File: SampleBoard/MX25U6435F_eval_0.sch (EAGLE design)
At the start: 7 parts, among them CN1 ARDUINO_COMPAT_IF, U1 MX25U6435F, U2 AE-FXMA108, U3 NCP563

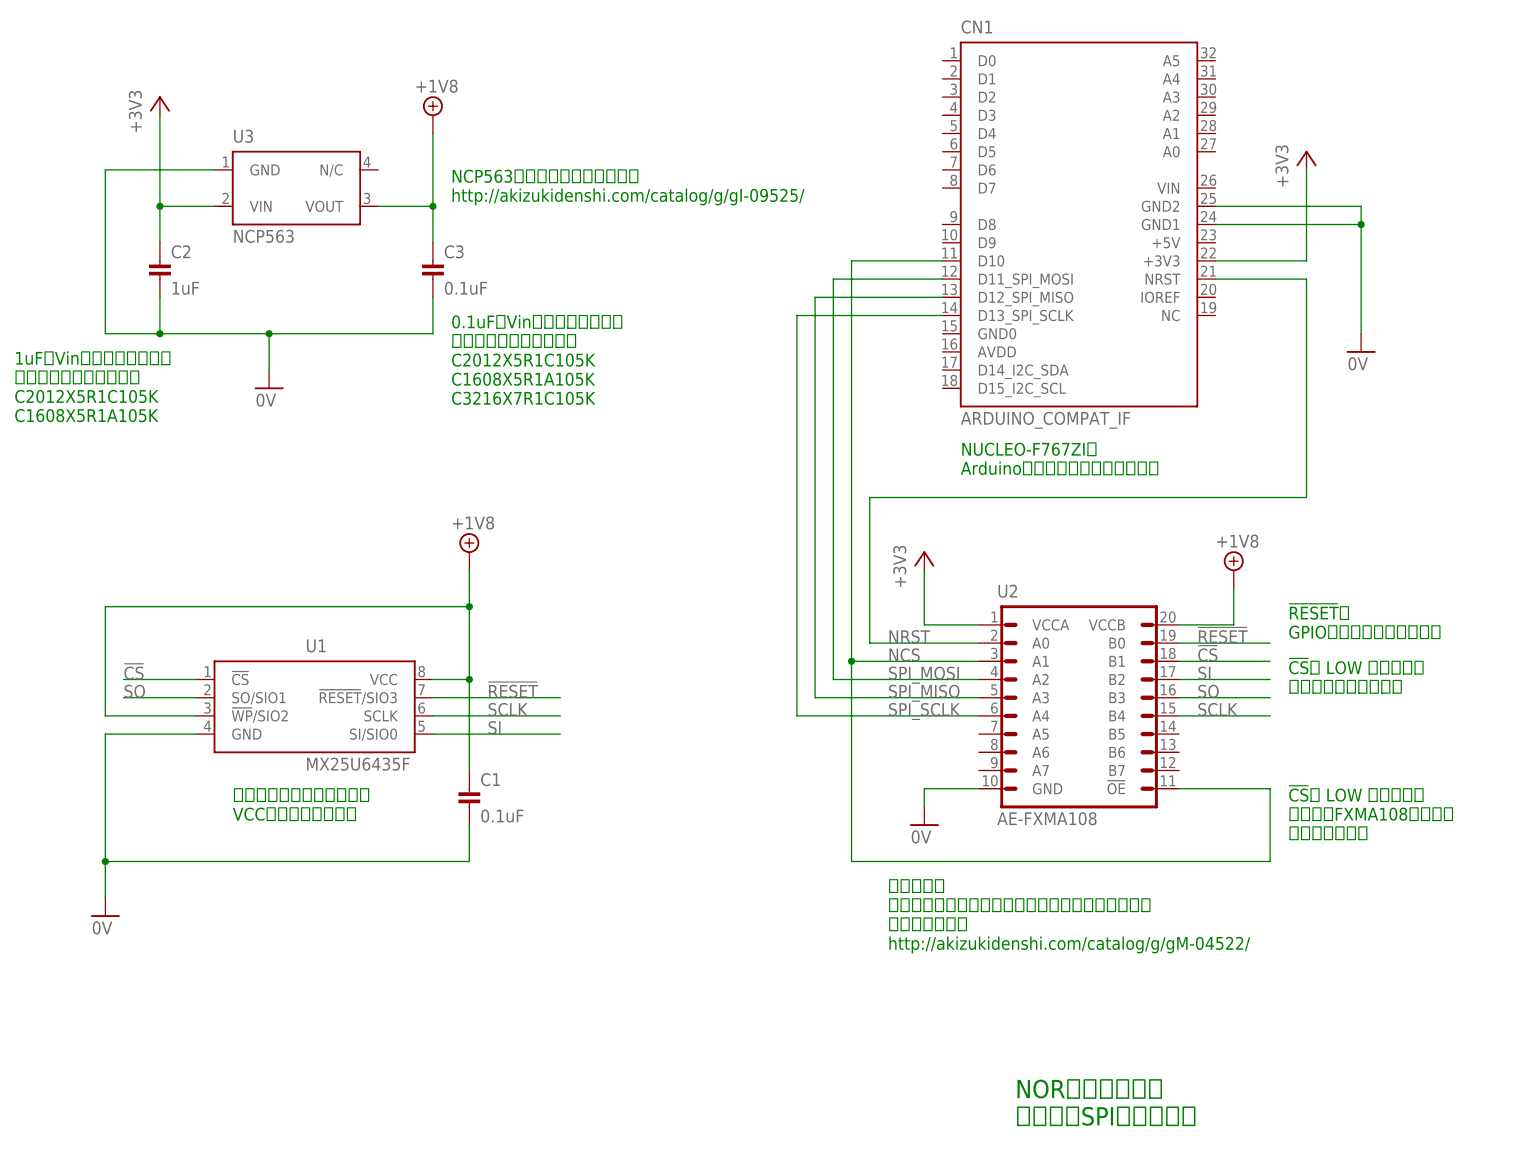
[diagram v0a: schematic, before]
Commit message: 評価回路を修正
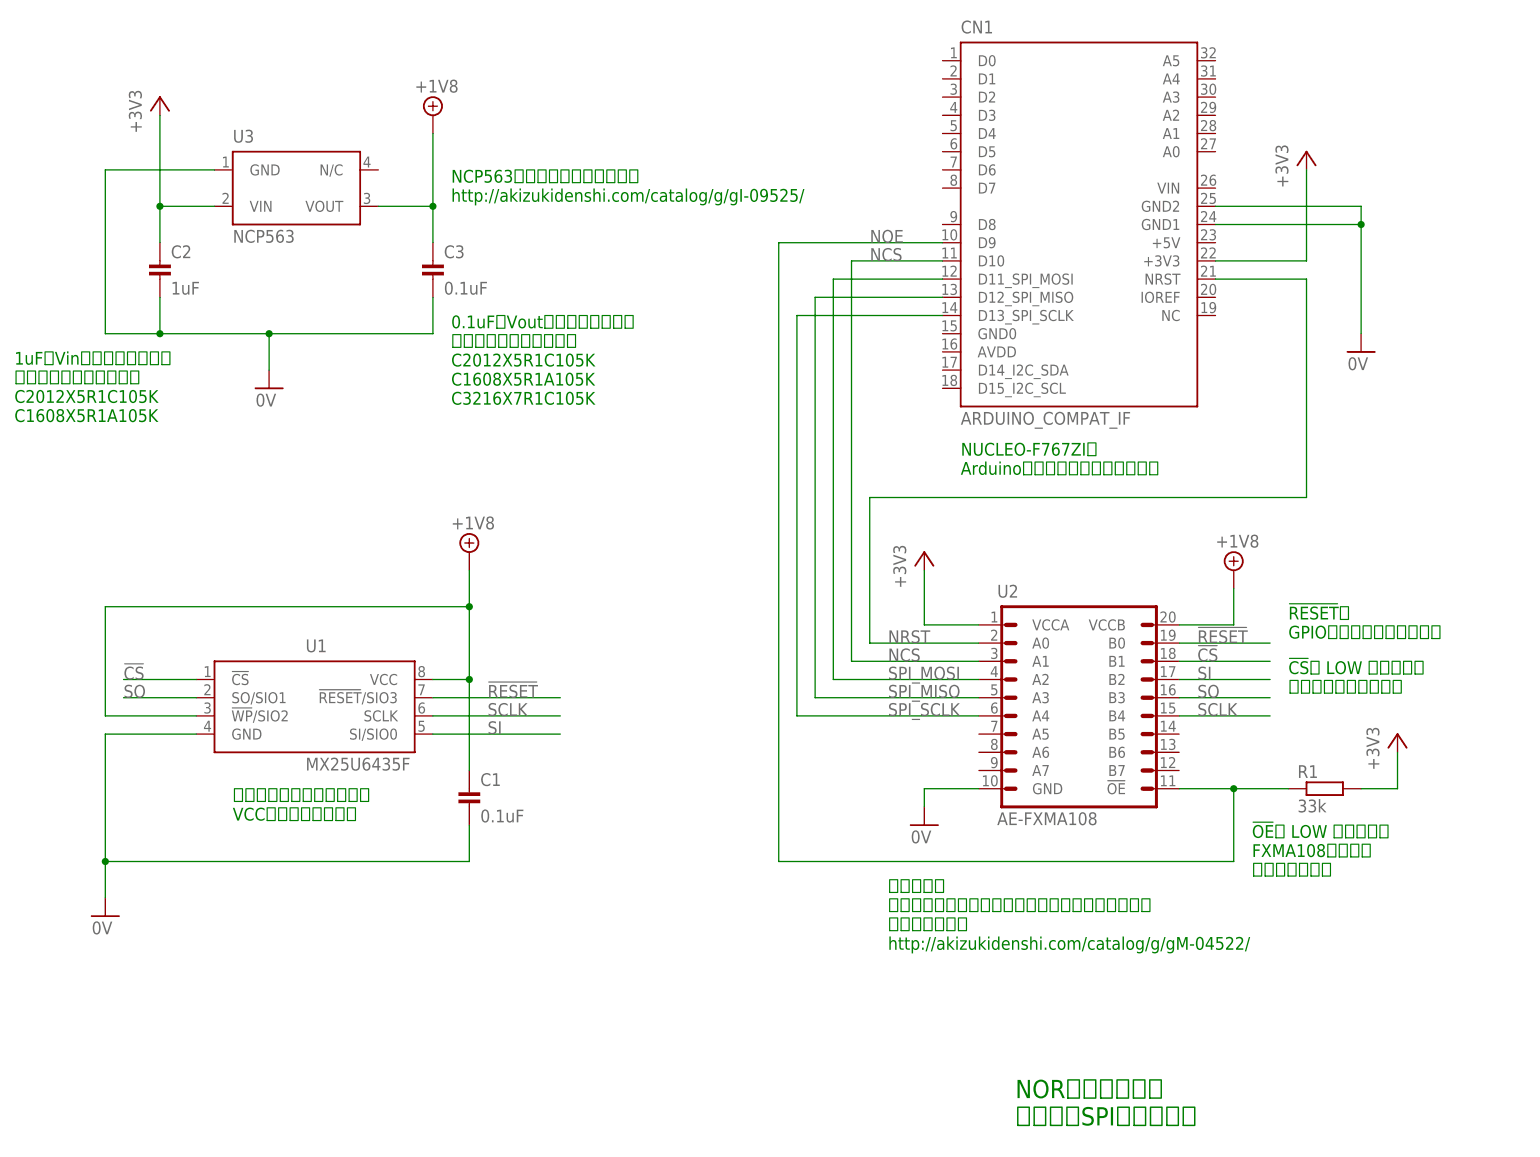
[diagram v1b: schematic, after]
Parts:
- added R1: 33k, Parts:RESISTOR_0603_DEV
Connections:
- new net NOE: CN1.D9, R1.1, U2.!OE!
- net +3V3: now also R1.2
- net NCS: no longer U2.!OE!
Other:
- note added: "!OE!に LOW を出力時は FXMA108のバスが 使用可能になる"
- note added: "0.1uFをVoutピンの近傍に設置 以下のいずれかを推奨： C2012X5R1C105K C1608X5R1A105K C3216X7R1C105K"
- note removed: "!CS!に LOW を出力時は 同時に、FXMA108のバスも 使用可能になる"
- note removed: "0.1uFをVinピンの近傍に設置 以下のいずれかを推奨： C2012X5R1C105K C1608X5R1A105K C3216X7R1C105K"
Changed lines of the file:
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@@
 <setting verticaltext="up"/>
 </settings>
-<grid distance="0.1" unitdist="inch" unit="inch" style="lines" multiple="1" display="no" altdistance="0.01" altunitdist="inch" altunit="inch"/>
+<grid distance="0.1" unitdist="inch" unit="inch" style="lines" multiple="1" display="yes" altdistance="0.01" altunitdist="inch" altunit="inch"/>
 <layers>
 <layer number="1" name="Top" color="4" fill="1" visible="no" active="no"/>
@@
 <part name="C2" library="Parts" deviceset="CAP" device="_0603_DEV" value="1uF"/>
 <part name="C3" library="Parts" deviceset="CAP" device="_0603_DEV" value="0.1uF"/>
+<part name="R1" library="Parts" deviceset="RESISTOR" device="_0603_DEV" value="33k"/>
+<part name="+3V4" library="Supply" deviceset="+3V3" device=""/>
 </parts>
 <sheets>
@@
 <text x="167.64" y="17.78" size="2.54" layer="91" align="top-left">NORフラッシュの
 標準的なSPI接続回路図</text>
-<text x="205.74" y="58.42" size="1.778" layer="91" align="top-left">!CS!に LOW を出力時は
-同時に、FXMA108のバスも
+<text x="200.66" y="53.34" size="1.778" layer="91" align="top-left">!OE!に LOW を出力時は
+FXMA108のバスが
 使用可能になる</text>
 <text x="27.94" y="119.38" size="1.778" layer="91" align="top-left">1uFをVinピンの近傍に設置
@@
 C2012X5R1C105K
 C1608X5R1A105K </text>
-<text x="88.9" y="124.46" size="1.778" layer="91" align="top-left">0.1uFをVinピンの近傍に設置
+<text x="88.9" y="124.46" size="1.778" layer="91" align="top-left">0.1uFをVoutピンの近傍に設置
 以下のいずれかを推奨：
 C2012X5R1C105K
@@
 <instance part="C2" gate="G$1" x="48.26" y="134.62"/>
 <instance part="C3" gate="G$1" x="86.36" y="134.62"/>
+<instance part="R1" gate="G$1" x="205.74" y="58.42"/>
+<instance part="+3V4" gate="G$1" x="220.98" y="66.04"/>
 </instances>
 <busses>
@@
 <wire x1="48.26" y1="152.4" x2="48.26" y2="139.7" width="0.1524" layer="91"/>
 <junction x="48.26" y="139.7"/>
+</segment>
+<segment>
+<pinref part="R1" gate="G$1" pin="2"/>
+<pinref part="+3V4" gate="G$1" pin="+3V3"/>
+<wire x1="215.9" y1="58.42" x2="220.98" y2="58.42" width="0.1524" layer="91"/>
+<wire x1="220.98" y1="58.42" x2="220.98" y2="63.5" width="0.1524" layer="91"/>
 </segment>
 </net>
@@
 <wire x1="144.78" y1="76.2" x2="162.56" y2="76.2" width="0.1524" layer="91"/>
 <label x="149.86" y="76.2" size="1.778" layer="95"/>
-<wire x1="144.78" y1="76.2" x2="144.78" y2="48.26" width="0.1524" layer="91"/>
-<junction x="144.78" y="76.2"/>
-<wire x1="144.78" y1="48.26" x2="203.2" y2="48.26" width="0.1524" layer="91"/>
-<wire x1="203.2" y1="48.26" x2="203.2" y2="58.42" width="0.1524" layer="91"/>
-<pinref part="U2" gate="G$1" pin="!OE!"/>
-<wire x1="203.2" y1="58.42" x2="190.5" y2="58.42" width="0.1524" layer="91"/>
+<label x="147.32" y="132.08" size="1.778" layer="95"/>
 </segment>
 </net>
@@
 </segment>
 </net>
+<net name="NOE" class="0">
+<segment>
+<pinref part="CN1" gate="G$1" pin="D9"/>
+<wire x1="157.48" y1="134.62" x2="134.62" y2="134.62" width="0.1524" layer="91"/>
+<label x="147.32" y="134.62" size="1.778" layer="95"/>
+<wire x1="134.62" y1="134.62" x2="134.62" y2="48.26" width="0.1524" layer="91"/>
+<pinref part="U2" gate="G$1" pin="!OE!"/>
+<pinref part="R1" gate="G$1" pin="1"/>
+<wire x1="190.5" y1="58.42" x2="198.12" y2="58.42" width="0.1524" layer="91"/>
+<wire x1="198.12" y1="58.42" x2="205.74" y2="58.42" width="0.1524" layer="91"/>
+<wire x1="134.62" y1="48.26" x2="198.12" y2="48.26" width="0.1524" layer="91"/>
+<wire x1="198.12" y1="48.26" x2="198.12" y2="58.42" width="0.1524" layer="91"/>
+<junction x="198.12" y="58.42"/>
+</segment>
+</net>

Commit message: 評価回路を修正
・PCBデザインはWIP
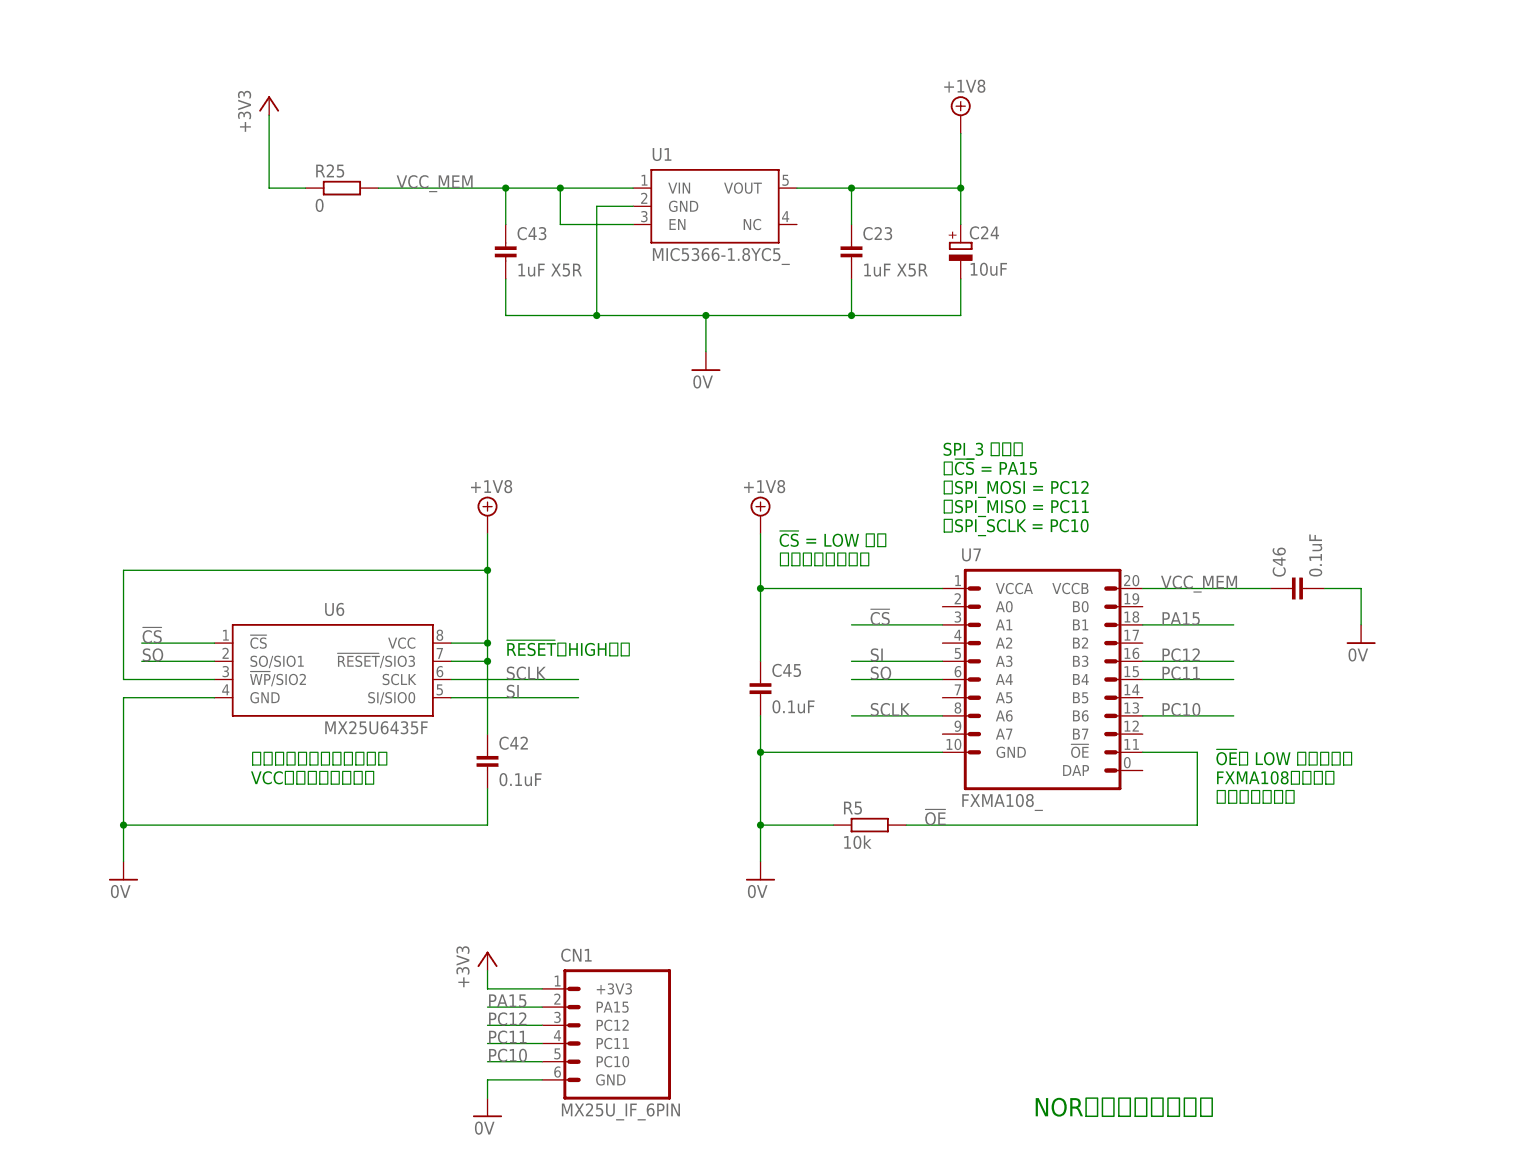
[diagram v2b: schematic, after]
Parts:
- removed C1, C3: 0.1uF, Parts:CAP_0603_DEV
- removed C2: 1uF, Parts:CAP_0603_DEV
- removed R1: 33k, Parts:RESISTOR_0603_DEV
- removed U2: AE-FXMA108, PartsForProto:AE-FXMA108
- removed U3: NCP563, Parts:NCP563
- added C23, C43: 1uF X5R, Parts:CAP_0603_DEV
- added C24: 10uF, Parts:TPST106K016R0800_
- added C42, C45, C46: 0.1uF, Parts:CAP_0603_DEV
- added R25: 0, Parts:RESISTOR_0603_DEV
- added R5: 10k, Parts:RESISTOR_0603_DEV
- added U6: MX25U6435F, Parts:MX25U6435F
- added U7: FXMA108_, Parts:FXMA108_
- CN1: value ARDUINO_COMPAT_IF -> MX25U_IF_6PIN; device PartsForProto:ARDUINO_COMPAT_IF -> PartsForProto:MX25U_IF_6PIN
- U1: value MX25U6435F -> MIC5366-1.8YC5_; device Parts:MX25U6435F -> Parts:MIC5366-1.8YC5_
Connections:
- removed net !RESET!: U1.!RESET!/SIO3, U2.B0
- removed net +18V: C1.1, C3.1, U1.!WP!/SIO2, U1.VCC, U2.VCCB, U3.VOUT
- removed net NCS: CN1.D10, U2.A1
- removed net NOE: CN1.D9, R1.1, U2.!OE!
- removed net NRST: CN1.NRST, U2.A0
- removed net SPI_MISO: CN1.D12_SPI_MISO, U2.A3
- removed net SPI_MOSI: CN1.D11_SPI_MOSI, U2.A2
- removed net SPI_SCLK: CN1.D13_SPI_SCLK, U2.A4
- new net !OE!: R5.2, U7.!OE!
- new net +1V8: C23.1, C24.+, C42.1, C45.1, U1.VOUT, U6.!RESET!/SIO3, U6.!WP!/SIO2, U6.VCC, U7.VCCA
- new net PA15: CN1.PA15, U7.B1
- new net PC10: CN1.PC10, U7.B6
- new net PC11: CN1.PC11, U7.B4
- new net PC12: CN1.PC12, U7.B3
- new net VCC_MEM: C43.1, C46.1, R25.2, U1.EN, U1.VIN, U7.VCCB
- net !CS!: now also U6.!CS, U7.A1; no longer U1.!CS, U2.B1
- net +3V3: now also R25.1; no longer C2.1, R1.2, U2.VCCA, U3.VIN
- net 0V: now also C23.2, C24.-, C42.2, C43.2, C45.2, C46.2, CN1.GND, R5.1, U6.GND, U7.GND; no longer C1.2, C2.2, C3.2, CN1.GND1, CN1.GND2, U2.GND, U3.GND
- net SCLK: now also U6.SCLK, U7.A6; no longer U1.SCLK, U2.B4
- net SI: now also U6.SI/SIO0, U7.A3; no longer U1.SI/SIO0, U2.B2
- net SO: now also U6.SO/SIO1, U7.A4; no longer U1.SO/SIO1, U2.B3
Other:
- note added: "!CS! = LOW 時は フラッシュ使用可"
- note added: "!RESET!はHIGH固定"
- note added: "NORフラッシュ回路図"
- note added: "SPI_3 を使用 ・!CS! = PA15 ・SPI_MOSI = PC12 ・SPI_MISO = PC11 ・SPI_SCLK = PC10"
- note removed: "!CS!に LOW を出力時は フラッシュが使用可能"
- note removed: "!RESET!は GPIOを使用しても制御可能"
- note removed: "0.1uFをVoutピンの近傍に設置 以下のいずれかを推奨： C2012X5R1C105K C1608X5R1A105K C3216X7R1C105K"
- note removed: "1uFをVinピンの近傍に設置 以下のいずれかを推奨： C2012X5R1C105K C1608X5R1A105K"
- note removed: "NCP563は秋月電子で入手可能。 http://akizukidenshi.com/catalog/g/gI-09525/"
- note removed: "NORフラッシュの 標準的なSPI接続回路図"
- note removed: "NUCLEO-F767ZIの Arduino互換ピンを使用する想定。"
- note removed: "秋月電子製 「８ビット双方向ロジックレベル変換モジュール」 を使うと便利。 http://akizukidenshi.com/catalog/g/gM-04522/"

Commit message: 配線を全面的に修正
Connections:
- net PC10: now also U7.B3; no longer U7.B6
- net PC11: now also U7.B5; no longer U7.B4
- net PC12: now also U7.B7; no longer U7.B3
- net SCLK: now also U7.A3; no longer U7.A6
- net SI: now also U7.A7; no longer U7.A3
- net SO: now also U7.A5; no longer U7.A4
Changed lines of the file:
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@@
 <setting verticaltext="up"/>
 </settings>
-<grid distance="0.1" unitdist="inch" unit="inch" style="lines" multiple="1" display="yes" altdistance="0.01" altunitdist="inch" altunit="inch"/>
+<grid distance="0.1" unitdist="inch" unit="inch" style="lines" multiple="1" display="no" altdistance="0.01" altunitdist="inch" altunit="inch"/>
 <layers>
 <layer number="1" name="Top" color="4" fill="1" visible="no" active="no"/>
@@
 </segment>
 <segment>
+<pinref part="U7" gate="G$1" pin="A7"/>
+<wire x1="157.48" y1="66.04" x2="144.78" y2="66.04" width="0.1524" layer="91"/>
+<label x="147.32" y="66.04" size="1.778" layer="95"/>
+</segment>
+</net>
+<net name="SO" class="0">
+<segment>
+<pinref part="U6" gate="G$1" pin="SO/SIO1"/>
+<wire x1="45.72" y1="76.2" x2="55.88" y2="76.2" width="0.1524" layer="91"/>
+<label x="45.72" y="76.2" size="1.778" layer="95"/>
+</segment>
+<segment>
+<pinref part="U7" gate="G$1" pin="A5"/>
+<wire x1="157.48" y1="71.12" x2="144.78" y2="71.12" width="0.1524" layer="91"/>
+<label x="147.32" y="71.12" size="1.778" layer="95"/>
+</segment>
+</net>
+<net name="SCLK" class="0">
+<segment>
+<pinref part="U6" gate="G$1" pin="SCLK"/>
+<wire x1="106.68" y1="73.66" x2="88.9" y2="73.66" width="0.1524" layer="91"/>
+<label x="96.52" y="73.66" size="1.778" layer="95"/>
+</segment>
+<segment>
 <pinref part="U7" gate="G$1" pin="A3"/>
 <wire x1="157.48" y1="76.2" x2="144.78" y2="76.2" width="0.1524" layer="91"/>
 <label x="147.32" y="76.2" size="1.778" layer="95"/>
-</segment>
-</net>
-<net name="SO" class="0">
-<segment>
-<pinref part="U6" gate="G$1" pin="SO/SIO1"/>
-<wire x1="45.72" y1="76.2" x2="55.88" y2="76.2" width="0.1524" layer="91"/>
-<label x="45.72" y="76.2" size="1.778" layer="95"/>
-</segment>
-<segment>
-<pinref part="U7" gate="G$1" pin="A4"/>
-<wire x1="157.48" y1="73.66" x2="144.78" y2="73.66" width="0.1524" layer="91"/>
-<label x="147.32" y="73.66" size="1.778" layer="95"/>
-</segment>
-</net>
-<net name="SCLK" class="0">
-<segment>
-<pinref part="U6" gate="G$1" pin="SCLK"/>
-<wire x1="106.68" y1="73.66" x2="88.9" y2="73.66" width="0.1524" layer="91"/>
-<label x="96.52" y="73.66" size="1.778" layer="95"/>
-</segment>
-<segment>
-<pinref part="U7" gate="G$1" pin="A6"/>
-<wire x1="157.48" y1="68.58" x2="144.78" y2="68.58" width="0.1524" layer="91"/>
-<label x="147.32" y="68.58" size="1.778" layer="95"/>
 </segment>
 </net>
@@
 <net name="PC12" class="0">
 <segment>
+<pinref part="CN1" gate="G$1" pin="PC12"/>
+<wire x1="93.98" y1="25.4" x2="101.6" y2="25.4" width="0.1524" layer="91"/>
+<label x="93.98" y="25.4" size="1.778" layer="95"/>
+</segment>
+<segment>
+<pinref part="U7" gate="G$1" pin="B7"/>
+<wire x1="185.42" y1="66.04" x2="198.12" y2="66.04" width="0.1524" layer="91"/>
+<label x="187.96" y="66.04" size="1.778" layer="95"/>
+</segment>
+</net>
+<net name="PC11" class="0">
+<segment>
+<pinref part="CN1" gate="G$1" pin="PC11"/>
+<wire x1="101.6" y1="22.86" x2="93.98" y2="22.86" width="0.1524" layer="91"/>
+<label x="93.98" y="22.86" size="1.778" layer="95"/>
+</segment>
+<segment>
+<pinref part="U7" gate="G$1" pin="B5"/>
+<wire x1="185.42" y1="71.12" x2="198.12" y2="71.12" width="0.1524" layer="91"/>
+<label x="187.96" y="71.12" size="1.778" layer="95"/>
+</segment>
+</net>
+<net name="PC10" class="0">
+<segment>
+<pinref part="CN1" gate="G$1" pin="PC10"/>
+<wire x1="101.6" y1="20.32" x2="93.98" y2="20.32" width="0.1524" layer="91"/>
+<label x="93.98" y="20.32" size="1.778" layer="95"/>
+</segment>
+<segment>
 <pinref part="U7" gate="G$1" pin="B3"/>
 <wire x1="185.42" y1="76.2" x2="198.12" y2="76.2" width="0.1524" layer="91"/>
 <label x="187.96" y="76.2" size="1.778" layer="95"/>
 </segment>
-<segment>
-<pinref part="CN1" gate="G$1" pin="PC12"/>
-<wire x1="93.98" y1="25.4" x2="101.6" y2="25.4" width="0.1524" layer="91"/>
-<label x="93.98" y="25.4" size="1.778" layer="95"/>
-</segment>
-</net>
-<net name="PC11" class="0">
-<segment>
-<pinref part="U7" gate="G$1" pin="B4"/>
-<wire x1="185.42" y1="73.66" x2="198.12" y2="73.66" width="0.1524" layer="91"/>
-<label x="187.96" y="73.66" size="1.778" layer="95"/>
-</segment>
-<segment>
-<pinref part="CN1" gate="G$1" pin="PC11"/>
-<wire x1="101.6" y1="22.86" x2="93.98" y2="22.86" width="0.1524" layer="91"/>
-<label x="93.98" y="22.86" size="1.778" layer="95"/>
-</segment>
-</net>
-<net name="PC10" class="0">
-<segment>
-<pinref part="U7" gate="G$1" pin="B6"/>
-<wire x1="185.42" y1="68.58" x2="198.12" y2="68.58" width="0.1524" layer="91"/>
-<label x="187.96" y="68.58" size="1.778" layer="95"/>
-</segment>
-<segment>
-<pinref part="CN1" gate="G$1" pin="PC10"/>
-<wire x1="101.6" y1="20.32" x2="93.98" y2="20.32" width="0.1524" layer="91"/>
-<label x="93.98" y="20.32" size="1.778" layer="95"/>
-</segment>
-</net>
+</net>
